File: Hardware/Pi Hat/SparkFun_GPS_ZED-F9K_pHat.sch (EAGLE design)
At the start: 46 parts, among them J1 QWIIC_RIGHT_ANGLE, J2 RASPBERRYPI-40-PIN-GPIO_PTH_N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, J4 U.FL, U1 UBLOX_ZED_F9K, U3 TRIPLE_BUFFER_74LVC3G07

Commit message: Adjust pi-hat design
* Moves jumpers to teh top
* moves labels for LEDs to teh Edge
* Moves USB and FTDI header to the bottom edge
* Fixes ESD protection IC routing
* Fixes RX/TX
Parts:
- removed R11: 27, SparkFun-Resistors:27OHM-0603-1/10W-1%
- added R6: 27, SparkFun-Resistors:27OHM-0603-1/10W-1%
- R13, R14, R2: value 1KOHM-0402-1/16W-1% -> 1k; device SparkFun-Resistors:1KOHM-0402-1/16W-1% -> SparkFun-Resistors:1KOHM-0603-1/10W-1%
- renumbered R10 to R7
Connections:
- net USB_D+ renamed N$9
- removed net N$16: D4.5, R7.1
- removed net N$17: D4.4, R11.1
- removed net USB_D-: D4.2, J8.D-
- new net N$10: D4.5, J8.VBUS
- new net N$11: D4.1, J8.D-
- new net N$14: U1.WHEEL_TKS
- new net N$15: U1.DIR
- new net N$6: D4.6, R7.1
- new net N$7: D4.4, R6.1
- net DPLUS: now also R6.2; no longer R11.2
- net GND: now also D4.2
- net RXI/MOSI: now also J2.TXO; no longer J2.RXI
- net TXO/MISO: now also J2.RXI; no longer J2.TXO
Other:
- note added: "Cut jumpers to remove pull-up resistors from data lines."
- note added: "I2C"
- note added: "SPI"
- note added: "USB - Aiding"
- note removed: "Power"
- note removed: "USB-C Connector"
- moved on the sheet: D4

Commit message: Replaces some 0402 components for 0603 on the pi-hat
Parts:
- C1: device SparkFun-Capacitors:0.1UF-0402-16V-10% -> SparkFun-Capacitors:0.1UF-0603-25V-(+80/-20%)
- R3, R4: value 2.2K -> 2.2k; device SparkFun-Resistors:2.2KOHM-0402-1/16W-1% -> SparkFun-Resistors:2.2KOHM-0603-1/10W-1%
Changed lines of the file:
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@@
 </classes>
 <parts>
-<part name="R3" library="SparkFun-Resistors" deviceset="2.2KOHM" device="-0402-1/16W-1%" value="2.2K"/>
-<part name="R4" library="SparkFun-Resistors" deviceset="2.2KOHM" device="-0402-1/16W-1%" value="2.2K"/>
+<part name="R3" library="SparkFun-Resistors" deviceset="2.2KOHM" device="-0603-1/10W-1%" value="2.2k"/>
+<part name="R4" library="SparkFun-Resistors" deviceset="2.2KOHM" device="-0603-1/10W-1%" value="2.2k"/>
 <part name="JP2" library="SparkFun-Jumpers" deviceset="JUMPER-SMT_3_2-NC_TRACE" device="_SILK" package3d_urn="urn:adsk.eagle:package:39289/1"/>
 <part name="J4" library="SparkFun-Connectors" deviceset="U.FL2PIN" device="" value="U.FL"/>
@@
 <part name="U1" library="classified" deviceset="UBLOX_ZED_F9K" device=""/>
 <part name="FRAME2" library="SparkFun-Aesthetics" deviceset="FRAME-LEDGER" device=""/>
-<part name="C1" library="SparkFun-Capacitors" deviceset="0.1UF" device="-0402-16V-10%" value="0.1uF"/>
+<part name="C1" library="SparkFun-Capacitors" deviceset="0.1UF" device="-0603-25V-(+80/-20%)" value="0.1uF"/>
 <part name="L1" library="SparkFun-Coils" deviceset="FERRITE_BEAD-120_OHM" device="-0402" value="3.9NH"/>
 <part name="C6" library="SparkFun-Capacitors" deviceset="1.0UF" device="-0402-16V-10%" value="1.0uF"/>

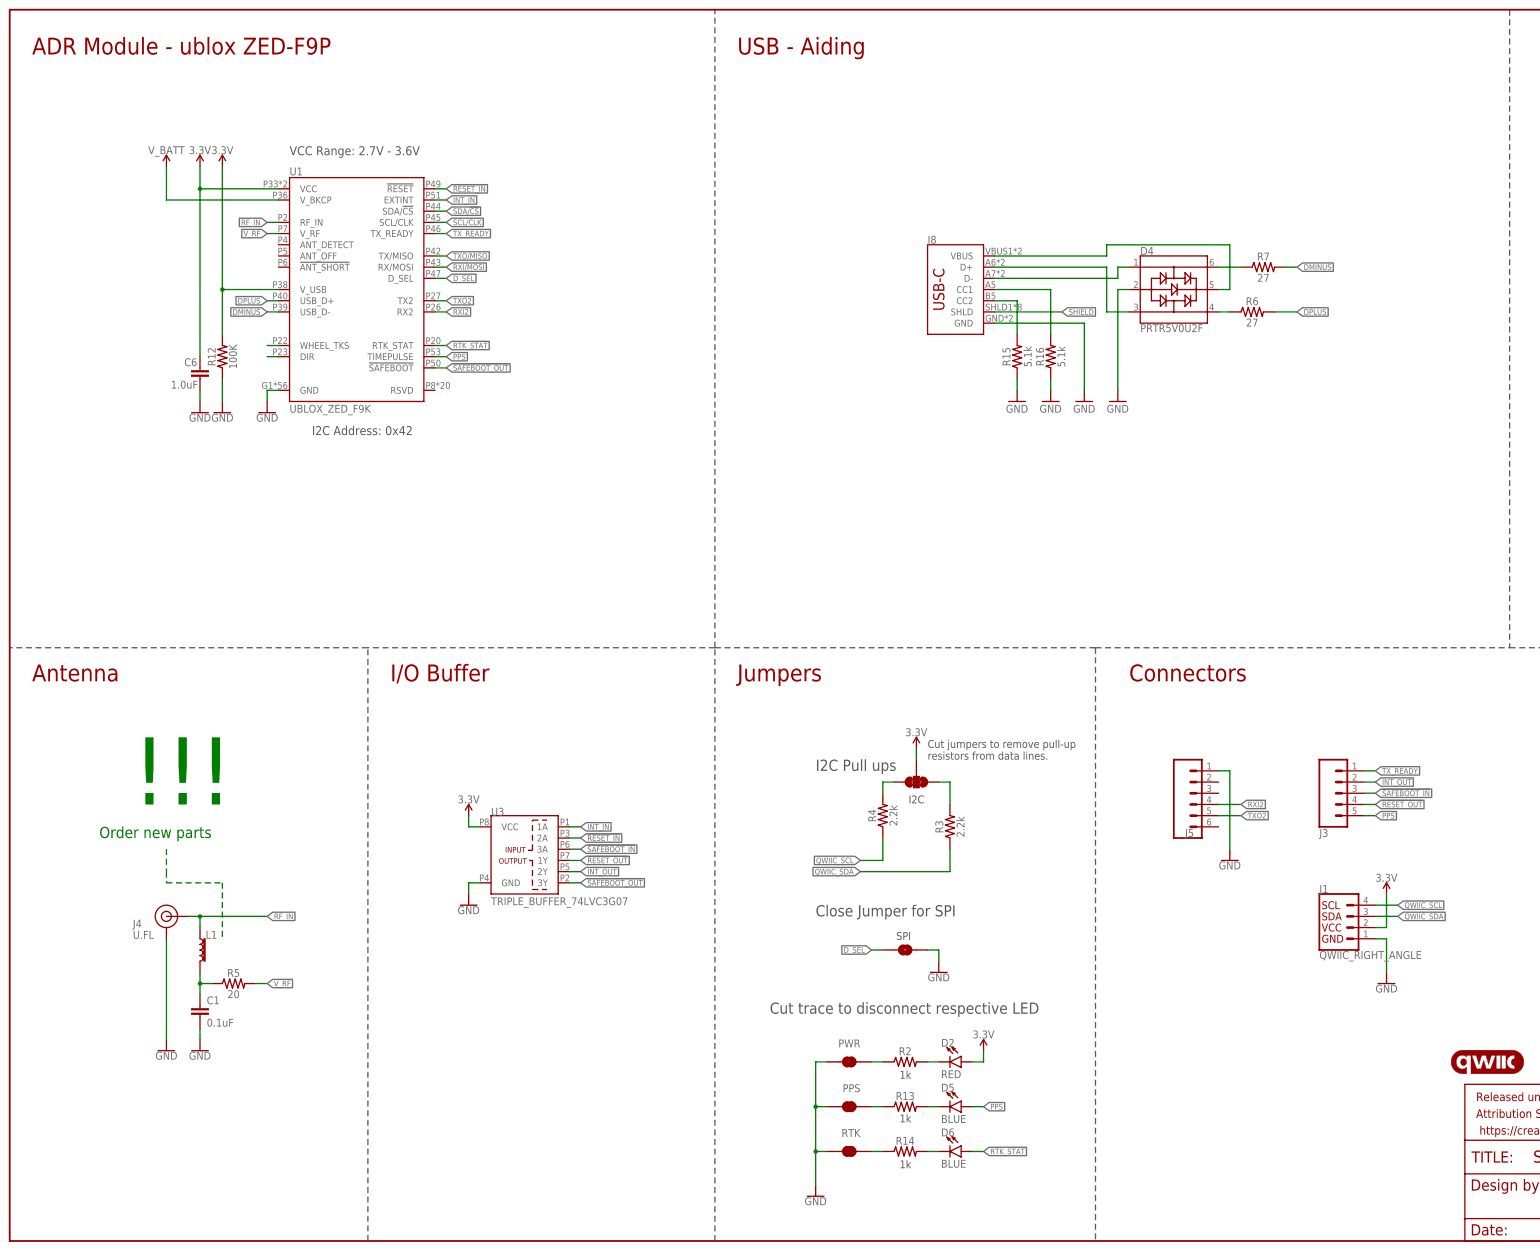
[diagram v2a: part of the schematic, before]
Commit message: Adds F9R datasheets, updates design with wheel ticks, direction pins, and adds 33 Ohm filtering resistors to all I/O
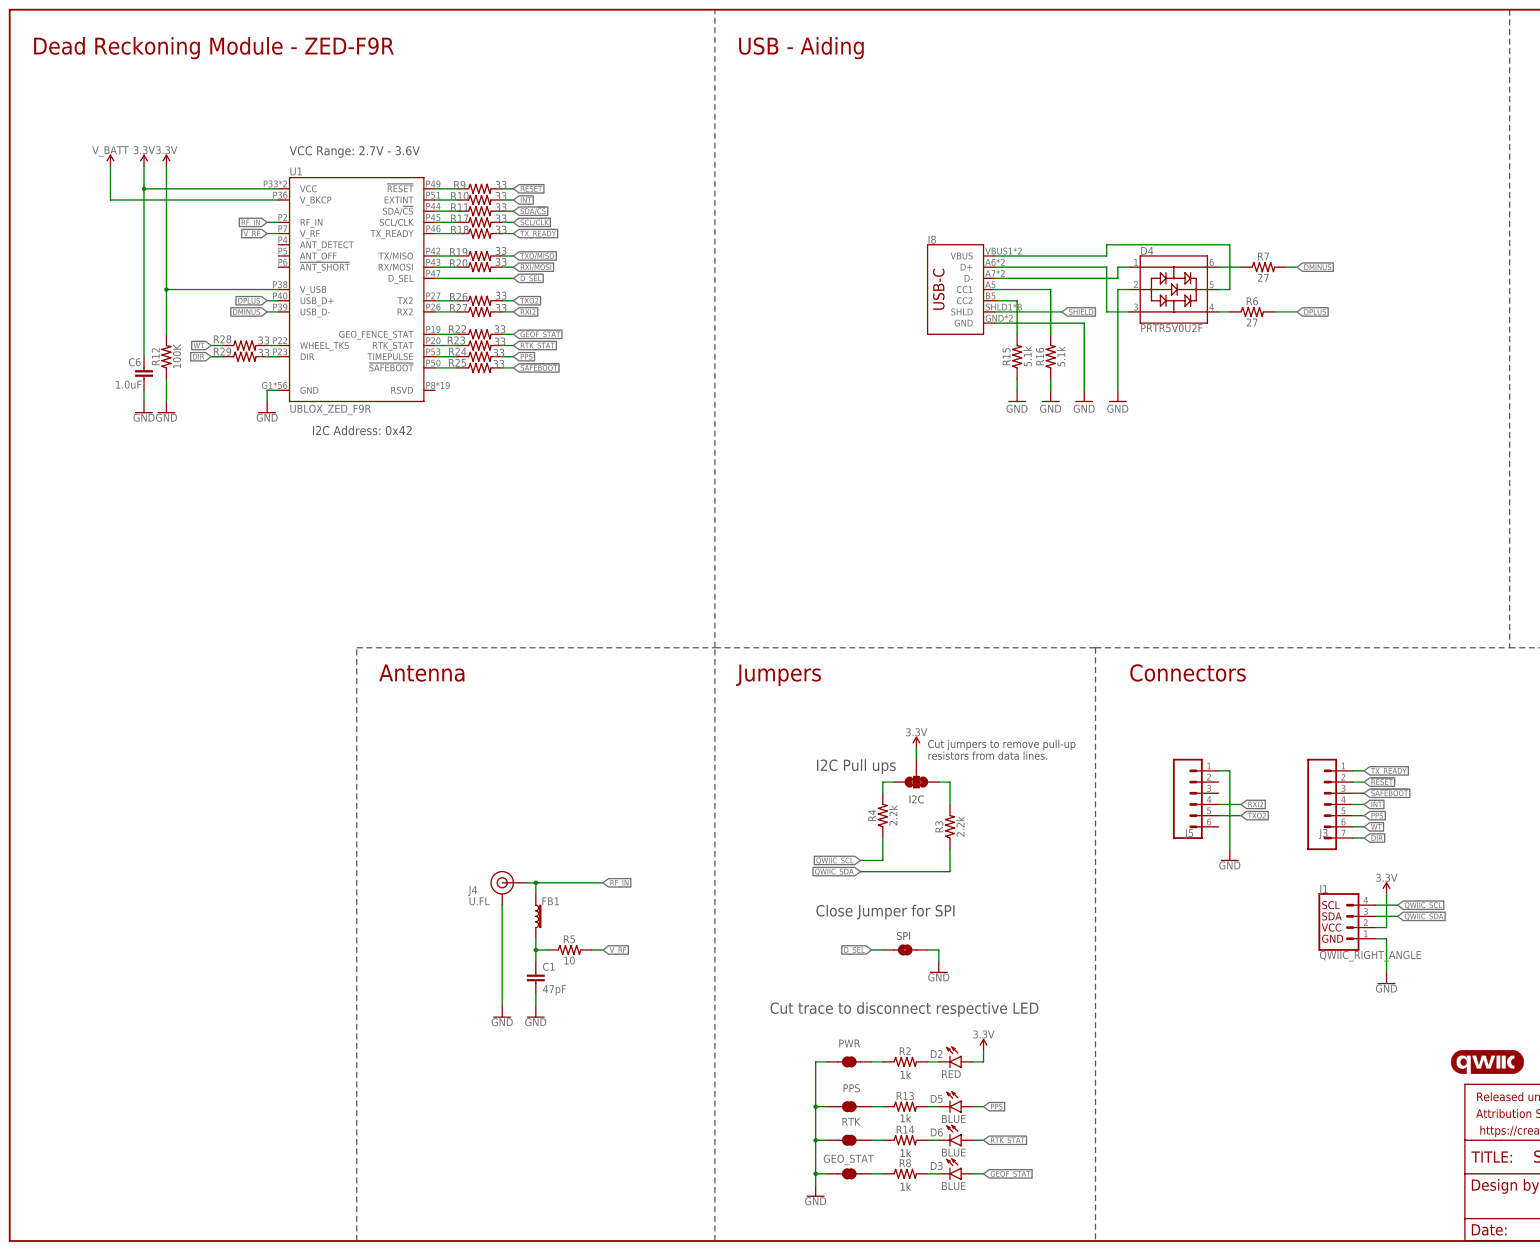
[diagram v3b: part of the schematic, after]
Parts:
- removed L1: 3.9NH, SparkFun-Coils:FERRITE_BEAD-120_OHM-0402
- removed U3: TRIPLE_BUFFER_74LVC3G07, classified:TRIPLE_BUFFER_74LVC3G07
- added D3: BLUE, SparkFun-LED:LED-BLUE0603
- added FB1: FERRITE_BEAD-120_OHM-0402, SparkFun-Coils:FERRITE_BEAD-120_OHM-0402
- added GEO_STAT: JUMPER-SMT_2_NC_TRACE_SILK, SparkFun-Jumpers:JUMPER-SMT_2_NC_TRACE_SILK
- added R10, R11, R17, R18, R19, R20, R22, R23, R24, R25, R26, R27, R28, R29, R9: 33, SparkFun-Resistors:33OHM-0603-1/10W-1%
- added R8: 1k, SparkFun-Resistors:1KOHM-0603-1/10W-1%
- C1: value 0.1uF -> 47pF; device SparkFun-Capacitors:0.1UF-0603-25V-(+80/-20%) -> SparkFun-Capacitors:47PF-0603-50V-5%
- J3: device SparkFun-Connectors:CONN_05NO_SILK -> SparkFun-Connectors:CONN_07NO_SILK
- R5: value 20 -> 10; device SparkFun-Resistors:20OHM-0603-1/10W-1% -> SparkFun-Resistors:10OHM-0603-1/10W-1%
- U1: value UBLOX_ZED_F9K -> UBLOX_ZED_F9R; device classified:UBLOX_ZED_F9K -> classified:UBLOX_ZED_F9R
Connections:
- removed net !RESET_IN: U1.!RESET!, U3.2A
- removed net !RESET_OUT: J3.4, U3.1Y
- removed net !SAFEBOOT_IN: J3.3, U3.3A
- removed net !SAFEBOOT_OUT: U1.!SAFEBOOT!, U3.3Y
- removed net INT_IN: U1.EXTINT, U3.1A
- removed net INT_OUT: J3.2, U3.2Y
- new net !RESET: J3.2, R9.2
- new net !SAFEBOOT: J3.3, R25.2
- new net DIR: J3.7, R29.1
- new net GEOF_STAT: D3.A, R22.2
- new net INT: J3.4, R10.2
- new net N$13: R9.1, U1.!RESET!
- new net N$16: GEO_STAT.2, R8.1
- new net N$17: D3.C, R8.2
- new net N$19: R17.1, U1.SCL/CLK
- new net N$20: R18.1, U1.TX_READY
- new net N$21: R19.1, U1.TX/MISO
- new net N$26: R20.1, U1.RX/MOSI
- new net N$28: R22.1, U1.GEO_FENCE_STAT
- new net N$29: R23.1, U1.RTK_STAT
- new net N$30: R24.1, U1.TIMEPULSE
- new net N$31: R25.1, U1.!SAFEBOOT!
- new net N$32: R26.1, U1.TX2
- new net N$33: R27.1, U1.RX2
- new net N$34: R28.2, U1.WHEEL_TKS
- new net N$35: R29.2, U1.DIR
- new net WT: J3.6, R28.1
- net 3.3V: no longer U3.VCC
- net GND: now also GEO_STAT.1; no longer U3.GND
- net N$14: now also R10.1, U1.EXTINT; no longer U1.WHEEL_TKS
- net N$15: now also R11.1, U1.SDA/!CS!; no longer U1.DIR
- net N$5: now also FB1.2; no longer L1.2
- net PPS: now also R24.2; no longer U1.TIMEPULSE
- net RF_IN: now also FB1.1; no longer L1.1
- net RTK_STAT: now also R23.2; no longer U1.RTK_STAT
- net RXI/MOSI: now also R20.2; no longer U1.RX/MOSI
- net RXI2: now also R27.2; no longer U1.RX2
- net SCL/CLK: now also R17.2; no longer U1.SCL/CLK
- net SDA/!CS: now also R11.2; no longer U1.SDA/!CS!
- net TXO/MISO: now also R19.2; no longer U1.TX/MISO
- net TXO2: now also R26.2; no longer U1.TX2
- net TX_READY: now also R18.2; no longer U1.TX_READY
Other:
- note added: "Dead Reckoning Module - ZED-F9R"
- note removed: "!!!"
- note removed: "ADR Module - ublox ZED-F9P"
- note removed: "I/O Buffer"
- note removed: "Order new parts"
- moved on the sheet: C1, C6, D6, J4, R12, R14, R5, RTK

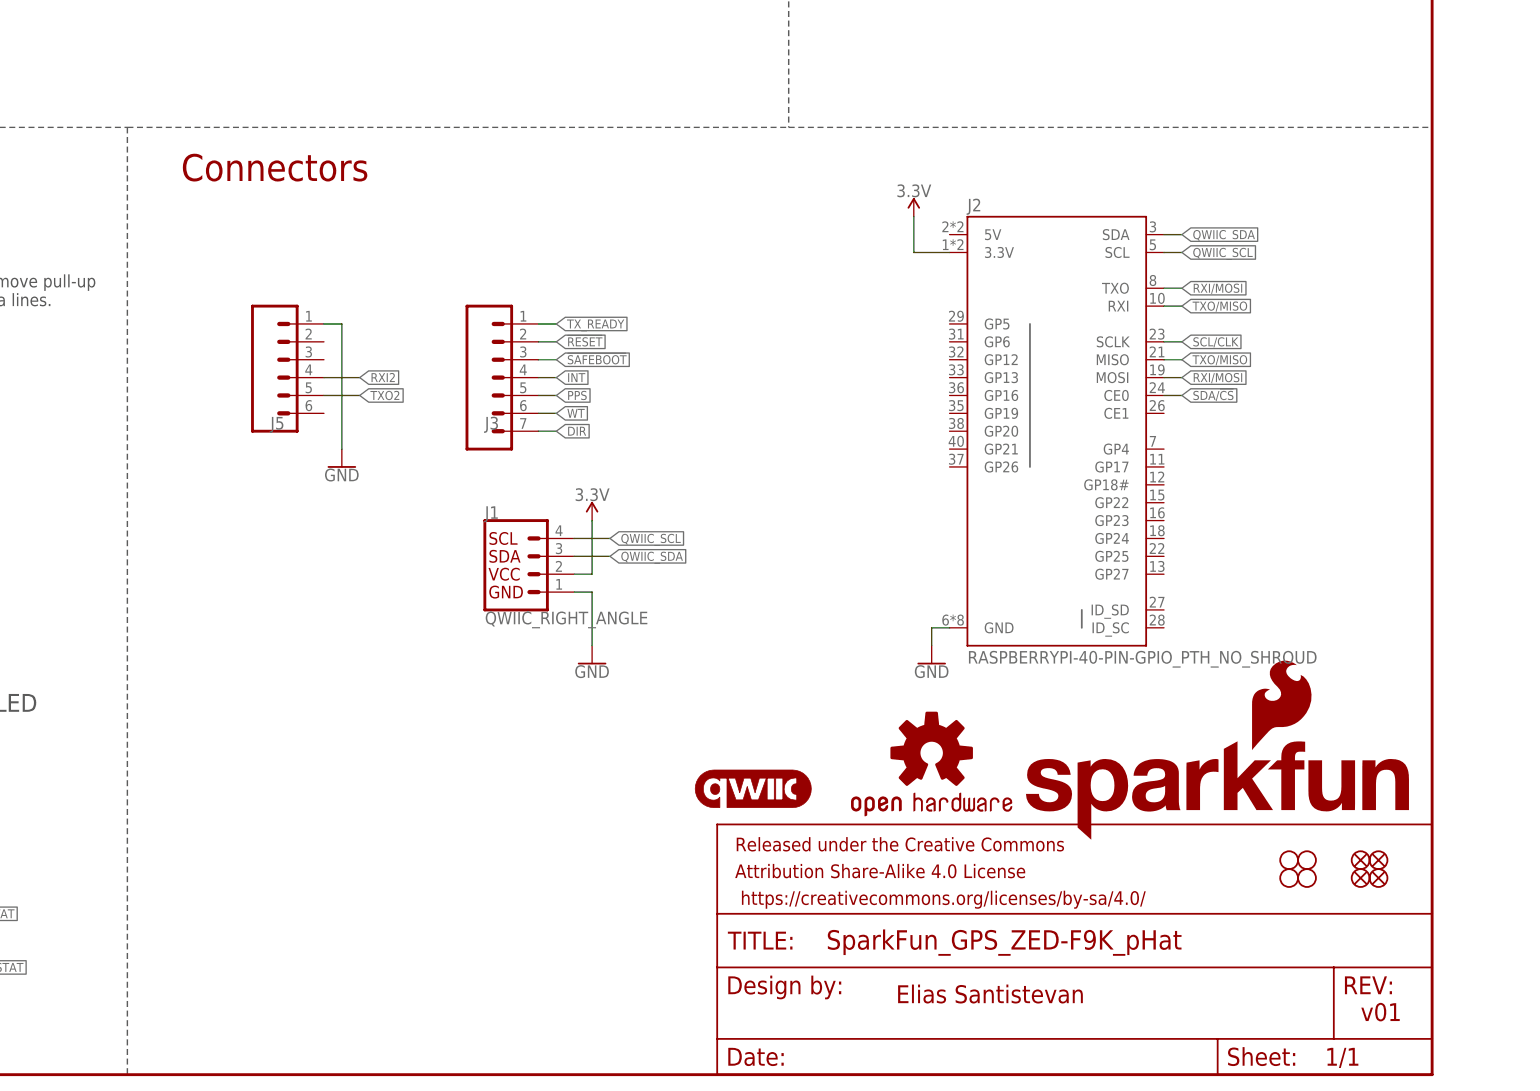
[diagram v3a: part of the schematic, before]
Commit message: Changes PTH header to double SMD male/femail combination
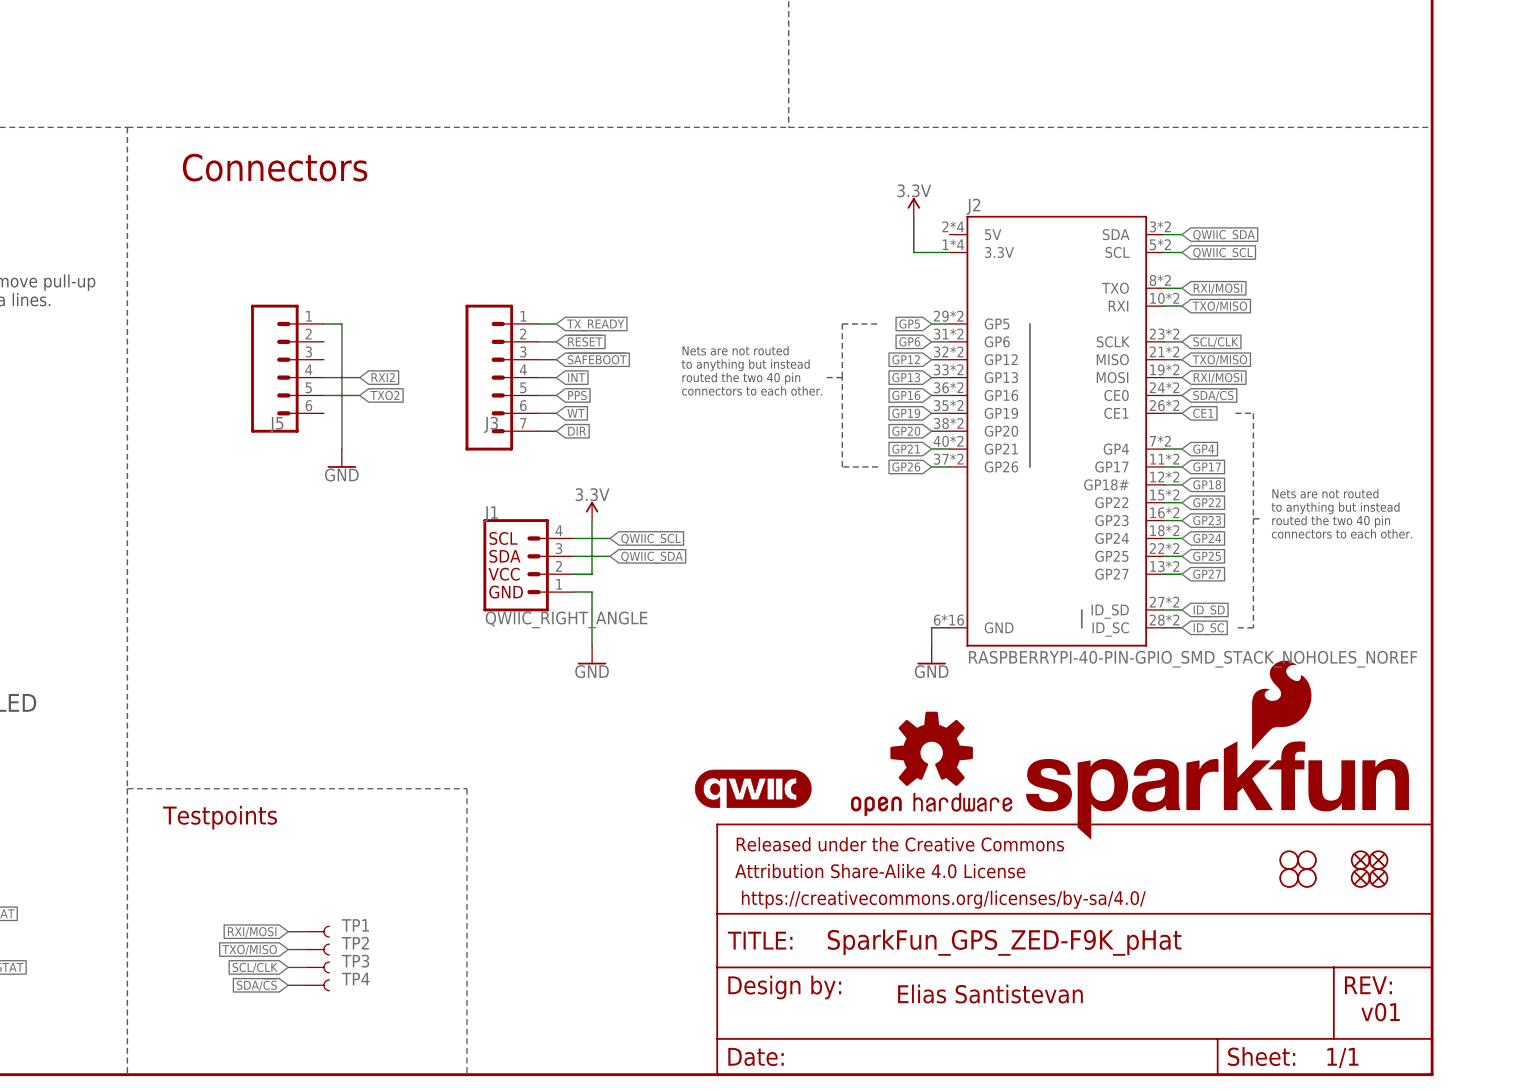
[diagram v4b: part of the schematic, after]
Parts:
- added TP1, TP2, TP3, TP4: TEST-POINT3X4, SparkFun-Connectors:TEST-POINT3X4
- J2: value RASPBERRYPI-40-PIN-GPIO_PTH_NO_SHROUD -> RASPBERRYPI-40-PIN-GPIO_SMD_STACK_NOHOLES_NOREF; device SparkFun-Connectors:RASPBERRYPI-40-PIN-GPIO_PTH_NO_SHROUD -> SparkFun-Connectors:RASPBERRYPI-40-PIN-GPIO_SMD_STACK_NOHOLES_NOREF
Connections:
- new net CE1: J2.CE1
- new net GP12: J2.GP12
- new net GP13: J2.GP13
- new net GP16: J2.GP16
- new net GP17: J2.GP17
- new net GP18: J2.GP18#
- new net GP19: J2.GP19
- new net GP20: J2.GP20
- new net GP21: J2.GP21
- new net GP22: J2.GP22
- new net GP23: J2.GP23
- new net GP24: J2.GP24
- new net GP25: J2.GP25
- new net GP26: J2.GP26
- new net GP27: J2.GP27
- new net GP4: J2.GP4
- new net GP5: J2.GP5
- new net GP6: J2.GP6
- new net ID_SC: J2.ID_SC
- new net ID_SD: J2.ID_SD
- net RXI/MOSI: now also TP1.1
- net SCL/CLK: now also TP3.1
- net SDA/!CS: now also TP4.1
- net TXO/MISO: now also TP2.1
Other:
- note added: "Nets are not routed to anything but instead routed the two 40 pin connectors to each other."
- note added: "Testpoints"
- moved on the sheet: J2
